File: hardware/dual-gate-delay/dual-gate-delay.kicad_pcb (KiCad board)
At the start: 4 copper layers, 40 x 100 mm, 55 parts, among them J1 MonoJack, J2 MonoJack, J3 MonoJack, J4 Conn_02x03_Odd_Even, J5 MonoJack, J6 MonoJack, J7 MonoJack, J8 Conn_02x03_Odd_Even, J9 Conn_02x05_Odd_Even, Q1 BC547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

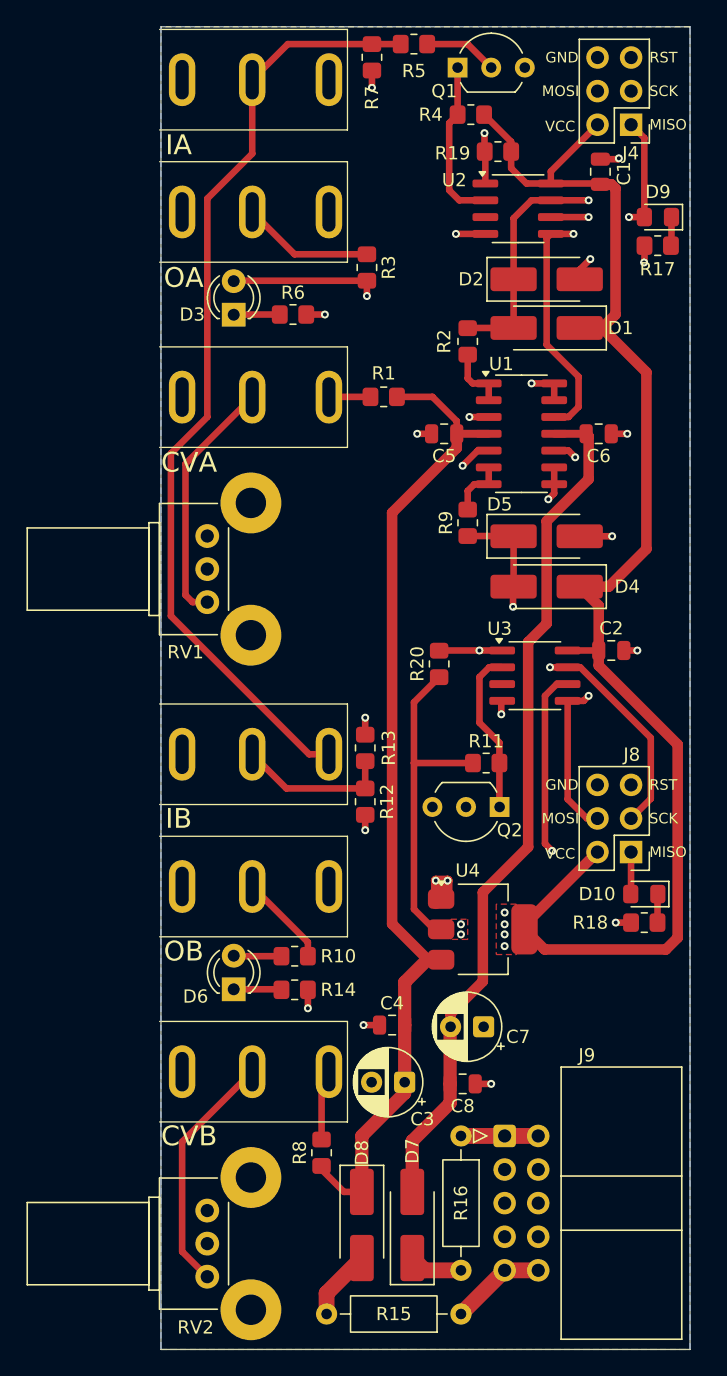
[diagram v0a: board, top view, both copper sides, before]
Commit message: Initial project for dual gate delay faceplate, small PBC revisions (SMT BJTs, moved LED)
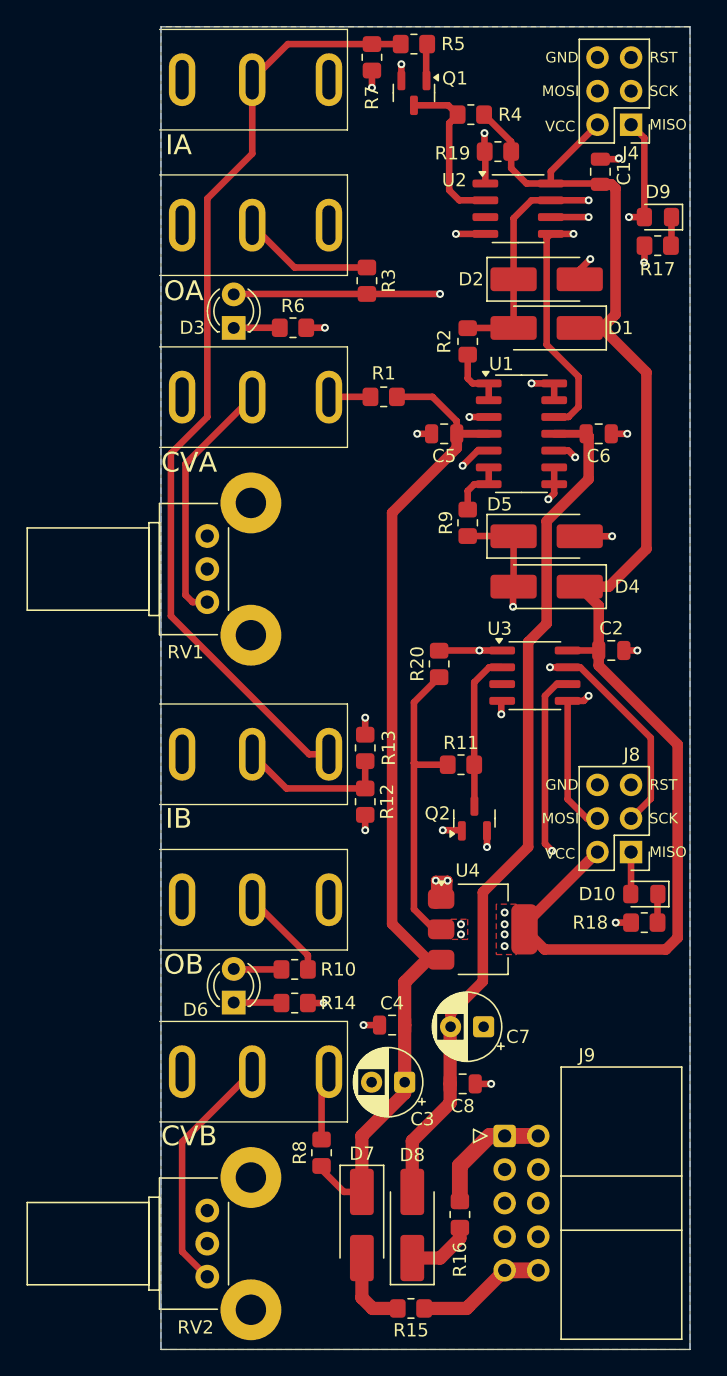
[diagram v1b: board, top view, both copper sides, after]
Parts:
- Q1, Q2: value BC547 -> BC847; footprint Package_TO_SOT_THT:TO-92_Inline_Wide -> Package_TO_SOT_SMD:SOT-23
- R15, R16: footprint Resistor_THT:R_Axial_DIN0207_L6.3mm_D2.5mm_P10.16mm_Horizontal -> Resistor_SMD:R_0805_2012Metric_Pad1.20x1.40mm_HandSolder
- moved R16 5.94 mm to (122.6, 139.8)
- moved Q1 3.82 mm to (119.1, 55.0), turned to -90 degrees
- moved R15 3.81 mm to (118.9, 146.9)
- moved Q2 2.09 mm to (123.7, 109.9), turned to 90 degrees
- moved R11 1.91 mm to (122.7, 105.8)
- moved D3 1.00 mm to (105.5, 72.8)
- moved D6 1.00 mm to (105.5, 123.8)
- moved J2 1.00 mm to (101.6, 65.0)
- moved J6 1.00 mm to (101.6, 116.0)
- moved R10 1.00 mm to (110.1, 121.3)
- moved R14 1.00 mm to (110.1, 123.8)
- moved R3 1.00 mm to (115.6, 69.2)
- moved R6 1.00 mm to (110.0, 72.8)
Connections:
- Q1 pad 1: /NGATE1_5V_A -> Net-(Q1-B)
- Q1 pad 2: Net-(Q1-B) -> GND
- Q1 pad 3: GND -> /NGATE1_5V_A
- Q2 pad 1: /NGATE1_5V_B -> Net-(Q2-B)
- Q2 pad 2: Net-(Q2-B) -> GND
- Q2 pad 3: GND -> /NGATE1_5V_B
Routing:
- net Net-(J9-Pin_1): track 5.84 -> 9.55 mm
- net Net-(Q1-B): track 5.58 -> 2.79 mm
- net Net-(J9-Pin_10): track 7.21 -> 9.82 mm
- net GND: track 28.4 -> 30.7 mm, vias 18 -> 20
- net +5V: track 134.1 -> 132.3 mm
- net Net-(D3-A): track 29.4 -> 28.3 mm
- net Net-(Q2-B): track 9.51 -> 8.48 mm, vias 1 -> 2
- net Net-(D6-A): track 51.8 -> 52.8 mm
- net Net-(D8-K): track 4.07 -> 5.02 mm
- net Net-(D7-A): track 5.34 -> 6.05 mm
- net /NGATE1_5V_B: track 12.5 -> 11.9 mm
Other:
- board text added: "idyllm CC BY-SA 4.0 v1.1.20251018"
- board text removed: "idyllm CC BY-SA 4.0 v1.0.20250917"
